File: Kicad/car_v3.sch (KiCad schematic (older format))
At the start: 1 part

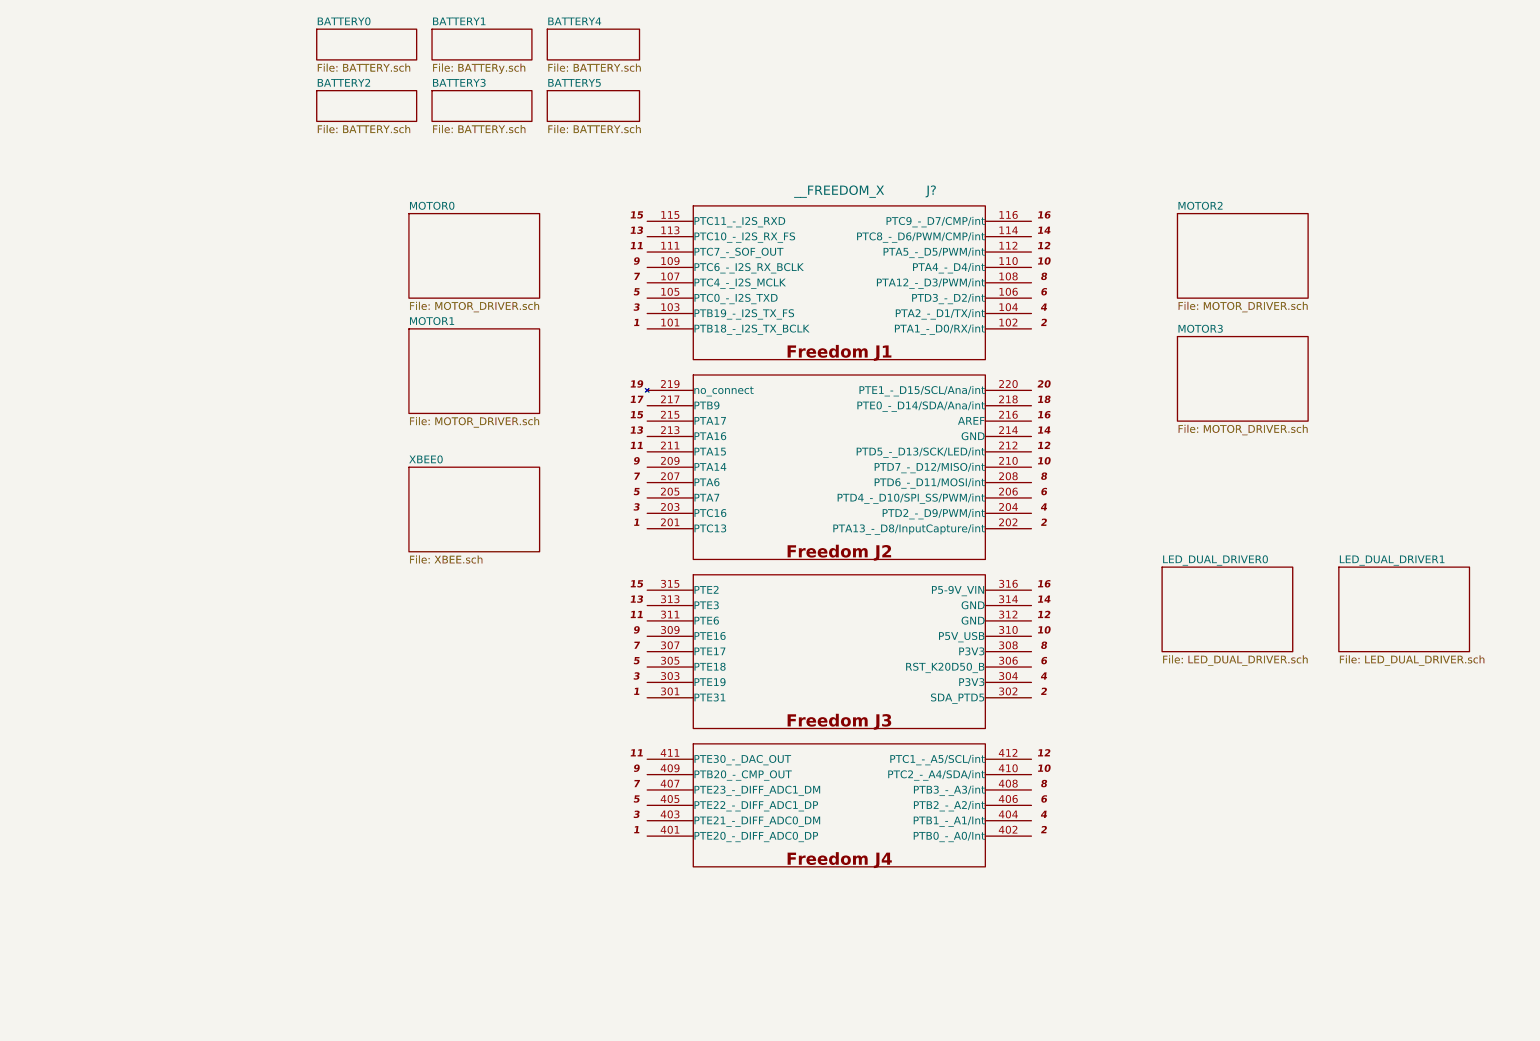
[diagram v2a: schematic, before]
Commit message: 
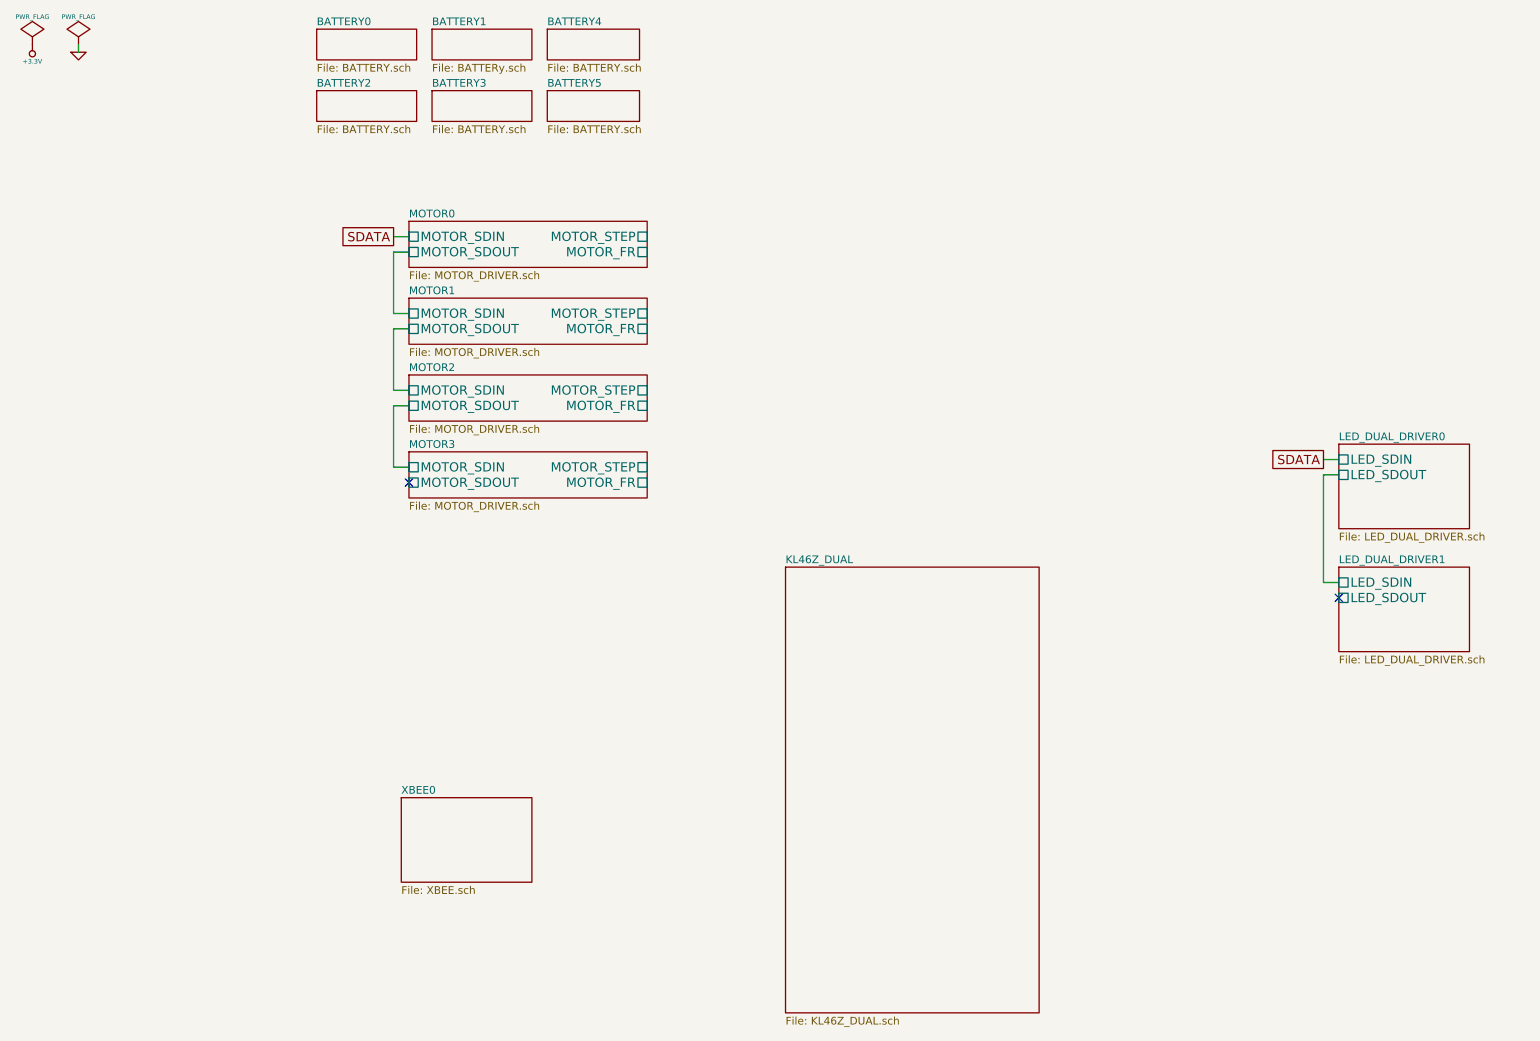
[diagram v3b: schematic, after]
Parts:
- removed J?: __FREEDOM_X, ~, symbol __FREEDOM_X
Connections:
- no-connect marks 0 -> 2
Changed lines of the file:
@@
 $Descr A4 11693 8268
 encoding utf-8
-Sheet 1 14
+Sheet 1 15
 Title ""
 Date "1 jun 2014"
@@
 Comment4 ""
 $EndDescr
-$Comp
-L __FREEDOM_X J?
-U 1 1 5387EDB5
-P 5850 4100
-F 0 "J?" H 6450 6550 60  0000 C CNN
-F 1 "__FREEDOM_X" H 5850 6550 60  0000 C CNN
-F 2 "~" H 5850 6550 60  0000 C CNN
-F 3 "~" H 5850 6550 60  0000 C CNN
-	1    5850 4100
-	1    0    0    -1
-$EndComp
 $Sheet
-S 3050 2550 850  550
+S 3050 2350 1550 300
 U 5387F728
 F0 "MOTOR1" 50
 F1 "MOTOR_DRIVER.sch" 50
+F2 "MOTOR_STEP" U R 4600 2450 60
+F3 "MOTOR_FR" U R 4600 2550 60
+F4 "MOTOR_SDIN" U L 3050 2450 60
+F5 "MOTOR_SDOUT" U L 3050 2550 60
 $EndSheet
 $Sheet
-S 8050 1800 850  550
+S 3050 2850 1550 300
 U 5387F76A
 F0 "MOTOR2" 50
 F1 "MOTOR_DRIVER.sch" 50
+F2 "MOTOR_STEP" U R 4600 2950 60
+F3 "MOTOR_FR" U R 4600 3050 60
+F4 "MOTOR_SDIN" U L 3050 2950 60
+F5 "MOTOR_SDOUT" U L 3050 3050 60
 $EndSheet
 $Sheet
-S 3050 1800 850  550
+S 3050 1850 1550 300
 U 5387F799
 F0 "MOTOR0" 50
 F1 "MOTOR_DRIVER.sch" 50
+F2 "MOTOR_STEP" U R 4600 1950 60
+F3 "MOTOR_FR" U R 4600 2050 60
+F4 "MOTOR_SDIN" U L 3050 1950 60
+F5 "MOTOR_SDOUT" U L 3050 2050 60
 $EndSheet
 $Sheet
-S 8050 2600 850  550
+S 3050 3350 1550 300
 U 5387F7BE
 F0 "MOTOR3" 50
 F1 "MOTOR_DRIVER.sch" 50
+F2 "MOTOR_STEP" U R 4600 3450 60
+F3 "MOTOR_FR" U R 4600 3550 60
+F4 "MOTOR_SDIN" U L 3050 3450 60
+F5 "MOTOR_SDOUT" U L 3050 3550 60
 $EndSheet
 $Sheet
-S 7950 4100 850  550
+S 9100 3300 850  550
 U 5387F99B
 F0 "LED_DUAL_DRIVER0" 50
 F1 "LED_DUAL_DRIVER.sch" 50
+F2 "LED_SDOUT" U L 9100 3500 60
+F3 "LED_SDIN" U L 9100 3400 60
 $EndSheet
 $Sheet
@@
 F0 "LED_DUAL_DRIVER1" 50
 F1 "LED_DUAL_DRIVER.sch" 50
+F2 "LED_SDOUT" U L 9100 4300 60
+F3 "LED_SDIN" U L 9100 4200 60
 $EndSheet
 $Sheet
-S 3050 3450 850  550
+S 3000 5600 850  550
 U 5387FD7B
 F0 "XBEE0" 50
@@
 F1 "BATTERY.sch" 50
 $EndSheet
+$Sheet
+S 5500 4100 1650 2900
+U 538A82BA
+F0 "KL46Z_DUAL" 50
+F1 "KL46Z_DUAL.sch" 50
+$EndSheet
+Wire Wire Line
+	3050 2050 2950 2050
+Wire Wire Line
+	2950 2050 2950 2450
+Wire Wire Line
+	2950 2450 3050 2450
+Wire Wire Line
+	3050 2550 2950 2550
+Wire Wire Line
+	2950 2550 2950 2950
+Wire Wire Line
+	2950 2950 3050 2950
+Wire Wire Line
+	3050 3050 2950 3050
+Wire Wire Line
+	2950 3050 2950 3450
+Wire Wire Line
+	2950 3450 3050 3450
+NoConn ~ 3050 3550
+Text GLabel 2950 1950 0    60   UnSpc ~ 0
+SDATA
+Wire Wire Line
+	2950 1950 3050 1950
+Text GLabel 9000 3400 0    60   UnSpc ~ 0
+SDATA
+Wire Wire Line
+	9100 3400 9000 3400
+Wire Wire Line
+	9100 3500 9000 3500
+Wire Wire Line
+	9000 3500 9000 4200
+Wire Wire Line
+	9000 4200 9100 4200
+NoConn ~ 9100 4300
+$Comp
+L PWR_FLAG #FLG01
+U 1 1 538B0DF3
+P 600 700
+F 0 "#FLG01" H 600 795 30  0001 C CNN
+F 1 "PWR_FLAG" H 600 880 30  0000 C CNN
+F 2 "" H 600 700 60  0000 C CNN
+F 3 "" H 600 700 60  0000 C CNN
+	1    600  700
+	1    0    0    -1
+$EndComp
+$Comp
+L +3.3V #PWR02
+U 1 1 538B11FE
+P 600 700
+F 0 "#PWR02" H 600 660 30  0001 C CNN
+F 1 "+3.3V" H 600 810 30  0000 C CNN
+F 2 "" H 600 700 60  0000 C CNN
+F 3 "" H 600 700 60  0000 C CNN
+	1    600  700
+	-1   0    0    1
+$EndComp
+$Comp
+L PWR_FLAG #FLG03
+U 1 1 538B120B
+P 900 700
+F 0 "#FLG03" H 900 795 30  0001 C CNN
+F 1 "PWR_FLAG" H 900 880 30  0000 C CNN
+F 2 "" H 900 700 60  0000 C CNN
+F 3 "" H 900 700 60  0000 C CNN
+	1    900  700
+	1    0    0    -1
+$EndComp
+$Comp
+L GND #PWR04
+U 1 1 538B1213
+P 900 750
+F 0 "#PWR04" H 900 750 30  0001 C CNN
+F 1 "GND" H 900 680 30  0001 C CNN
+F 2 "" H 900 750 60  0000 C CNN
+F 3 "" H 900 750 60  0000 C CNN
+	1    900  750
+	1    0    0    -1
+$EndComp
+Wire Wire Line
+	900  700  900  750
 $EndSCHEMATC

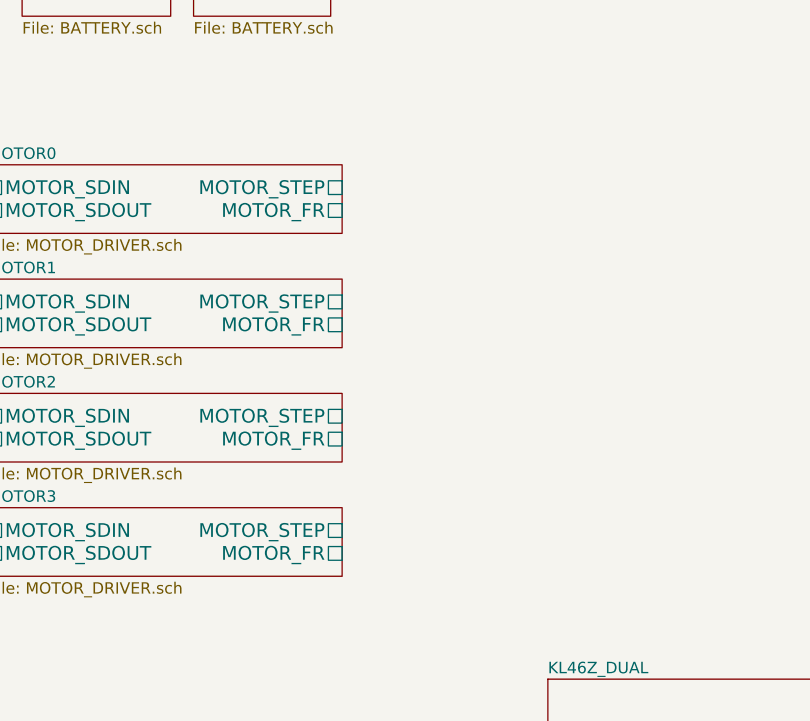
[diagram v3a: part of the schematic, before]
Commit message: 
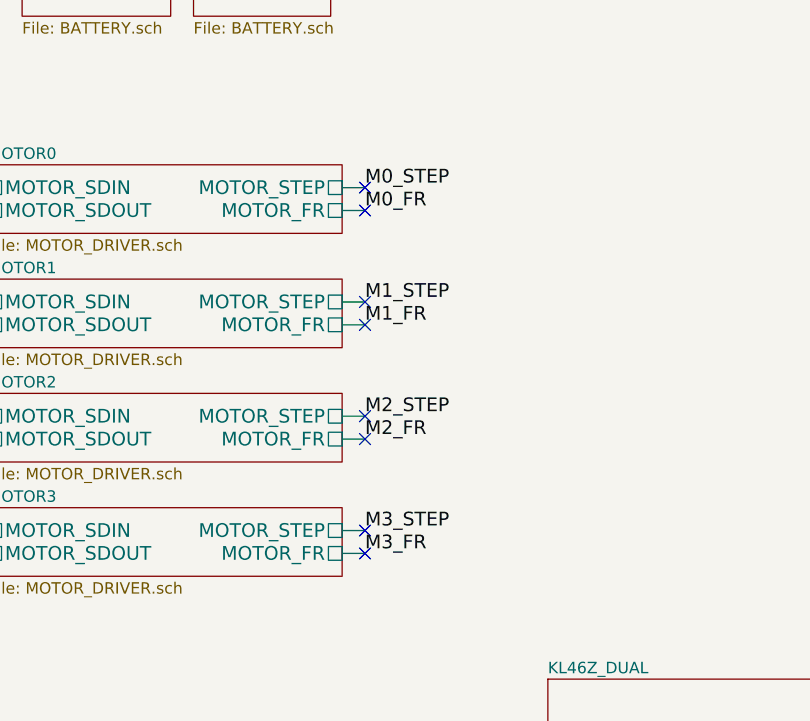
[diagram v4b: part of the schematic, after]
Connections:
- no-connect marks 2 -> 10
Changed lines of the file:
@@
 Wire Wire Line
 	900  700  900  750
+Text Label 4700 1950 0    60   ~ 0
+M0_STEP
+Text Label 4700 2450 0    60   ~ 0
+M1_STEP
+Text Label 4700 2950 0    60   ~ 0
+M2_STEP
+Text Label 4700 3450 0    60   ~ 0
+M3_STEP
+Text Label 4700 2050 0    60   ~ 0
+M0_FR
+Text Label 4700 2550 0    60   ~ 0
+M1_FR
+Text Label 4700 3050 0    60   ~ 0
+M2_FR
+Text Label 4700 3550 0    60   ~ 0
+M3_FR
+Wire Wire Line
+	4700 1950 4600 1950
+Wire Wire Line
+	4600 2050 4700 2050
+Wire Wire Line
+	4600 2450 4700 2450
+Wire Wire Line
+	4600 2550 4700 2550
+Wire Wire Line
+	4600 2950 4700 2950
+Wire Wire Line
+	4600 3050 4700 3050
+Wire Wire Line
+	4600 3450 4700 3450
+Wire Wire Line
+	4600 3550 4700 3550
+NoConn ~ 4700 1950
+NoConn ~ 4700 2450
+NoConn ~ 4700 2950
+NoConn ~ 4700 3450
+NoConn ~ 4700 2050
+NoConn ~ 4700 2550
+NoConn ~ 4700 3050
+NoConn ~ 4700 3550
 $EndSCHEMATC
